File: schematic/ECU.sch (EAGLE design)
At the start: 21 parts, among them J1 Break, J2 COMM, J3 PWS, J4 DISPLAY, J5 THROTTLE, J6 LED, J7 SPEED, Q1 NMOSFETSOT23, Q2 NMOSFETSOT23, Q4 PMOSFET_BSS84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

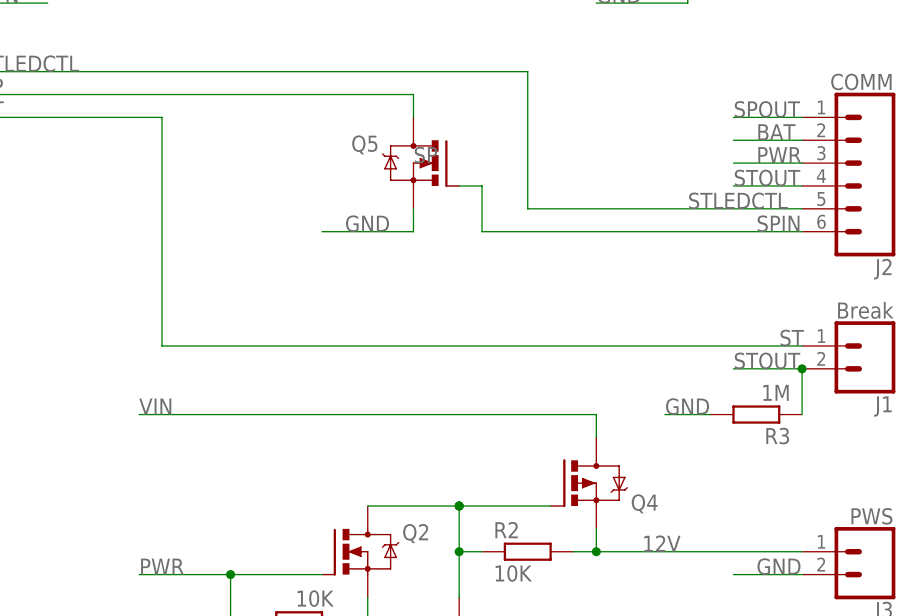
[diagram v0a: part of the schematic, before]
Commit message: Fix stop sensor schematics
- Make stop sensor LOW by default, connected to GND.
- Add control transistor for break on BLDC
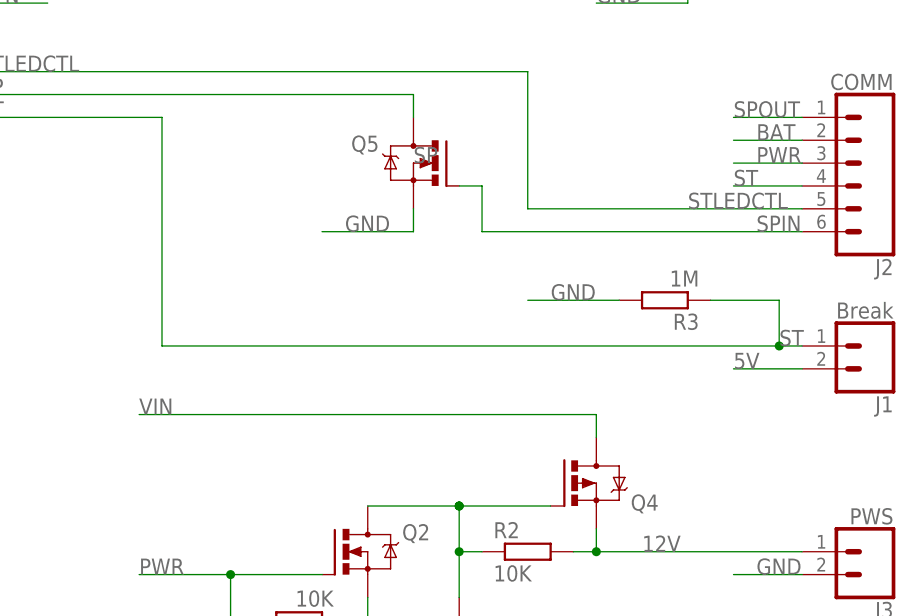
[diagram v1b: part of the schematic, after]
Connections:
- removed net STOUT: J1.2, J2.4, R3.1
- net 5V: now also J1.2
- net ST: now also J2.4, R3.1
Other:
- moved on the sheet: R3
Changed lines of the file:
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@@
 <attribute name="VALUE" x="-30.48" y="40.386" size="1.778" layer="96" font="vector" rot="MR270"/>
 </instance>
-<instance part="R3" gate="G$1" x="132.08" y="22.86" smashed="yes" rot="R180">
-<attribute name="NAME" x="135.89" y="21.3614" size="1.778" layer="95" rot="R180"/>
-<attribute name="VALUE" x="135.89" y="26.162" size="1.778" layer="96" rot="R180"/>
+<instance part="R3" gate="G$1" x="121.92" y="35.56" smashed="yes" rot="R180">
+<attribute name="NAME" x="125.73" y="34.0614" size="1.778" layer="95" rot="R180"/>
+<attribute name="VALUE" x="125.73" y="38.862" size="1.778" layer="96" rot="R180"/>
 </instance>
 </instances>
@@
 <segment>
 <pinref part="R3" gate="G$1" pin="2"/>
-<wire x1="127" y1="22.86" x2="121.92" y2="22.86" width="0.1524" layer="91"/>
-<label x="121.92" y="22.86" size="1.778" layer="95"/>
+<wire x1="116.84" y1="35.56" x2="106.68" y2="35.56" width="0.1524" layer="91"/>
+<label x="109.22" y="35.56" size="1.778" layer="95"/>
 </segment>
 </net>
@@
 <label x="10.16" y="93.98" size="1.778" layer="95"/>
 </segment>
+<segment>
+<pinref part="J1" gate="G$1" pin="2"/>
+<label x="129.54" y="27.94" size="1.778" layer="95"/>
+<wire x1="137.16" y1="27.94" x2="129.54" y2="27.94" width="0.1524" layer="91"/>
+</segment>
 </net>
 <net name="THIN" class="0">
@@
 <label x="134.62" y="30.48" size="1.778" layer="95"/>
 <label x="45.72" y="55.88" size="1.778" layer="95"/>
-<wire x1="137.16" y1="30.48" x2="66.04" y2="30.48" width="0.1524" layer="91"/>
+<wire x1="137.16" y1="30.48" x2="134.62" y2="30.48" width="0.1524" layer="91"/>
+<wire x1="134.62" y1="30.48" x2="66.04" y2="30.48" width="0.1524" layer="91"/>
 <wire x1="66.04" y1="55.88" x2="45.72" y2="55.88" width="0.1524" layer="91"/>
 <pinref part="U$2" gate="G$1" pin="D2"/>
 <wire x1="66.04" y1="55.88" x2="66.04" y2="30.48" width="0.1524" layer="91"/>
+<pinref part="R3" gate="G$1" pin="1"/>
+<wire x1="127" y1="35.56" x2="134.62" y2="35.56" width="0.1524" layer="91"/>
+<wire x1="134.62" y1="35.56" x2="134.62" y2="30.48" width="0.1524" layer="91"/>
+<junction x="134.62" y="30.48"/>
+</segment>
+<segment>
+<pinref part="J2" gate="G$1" pin="4"/>
+<wire x1="137.16" y1="48.26" x2="129.54" y2="48.26" width="0.1524" layer="91"/>
+<label x="129.54" y="48.26" size="1.778" layer="95"/>
 </segment>
 </net>
@@
 </segment>
 </net>
-<net name="STOUT" class="0">
-<segment>
-<pinref part="J1" gate="G$1" pin="2"/>
-<wire x1="137.16" y1="27.94" x2="137.16" y2="22.86" width="0.1524" layer="91"/>
-<label x="129.54" y="27.94" size="1.778" layer="95"/>
-<pinref part="R3" gate="G$1" pin="1"/>
-<wire x1="137.16" y1="27.94" x2="129.54" y2="27.94" width="0.1524" layer="91"/>
-<junction x="137.16" y="27.94"/>
-</segment>
-<segment>
-<pinref part="J2" gate="G$1" pin="4"/>
-<wire x1="137.16" y1="48.26" x2="129.54" y2="48.26" width="0.1524" layer="91"/>
-<label x="129.54" y="48.26" size="1.778" layer="95"/>
-</segment>
-</net>

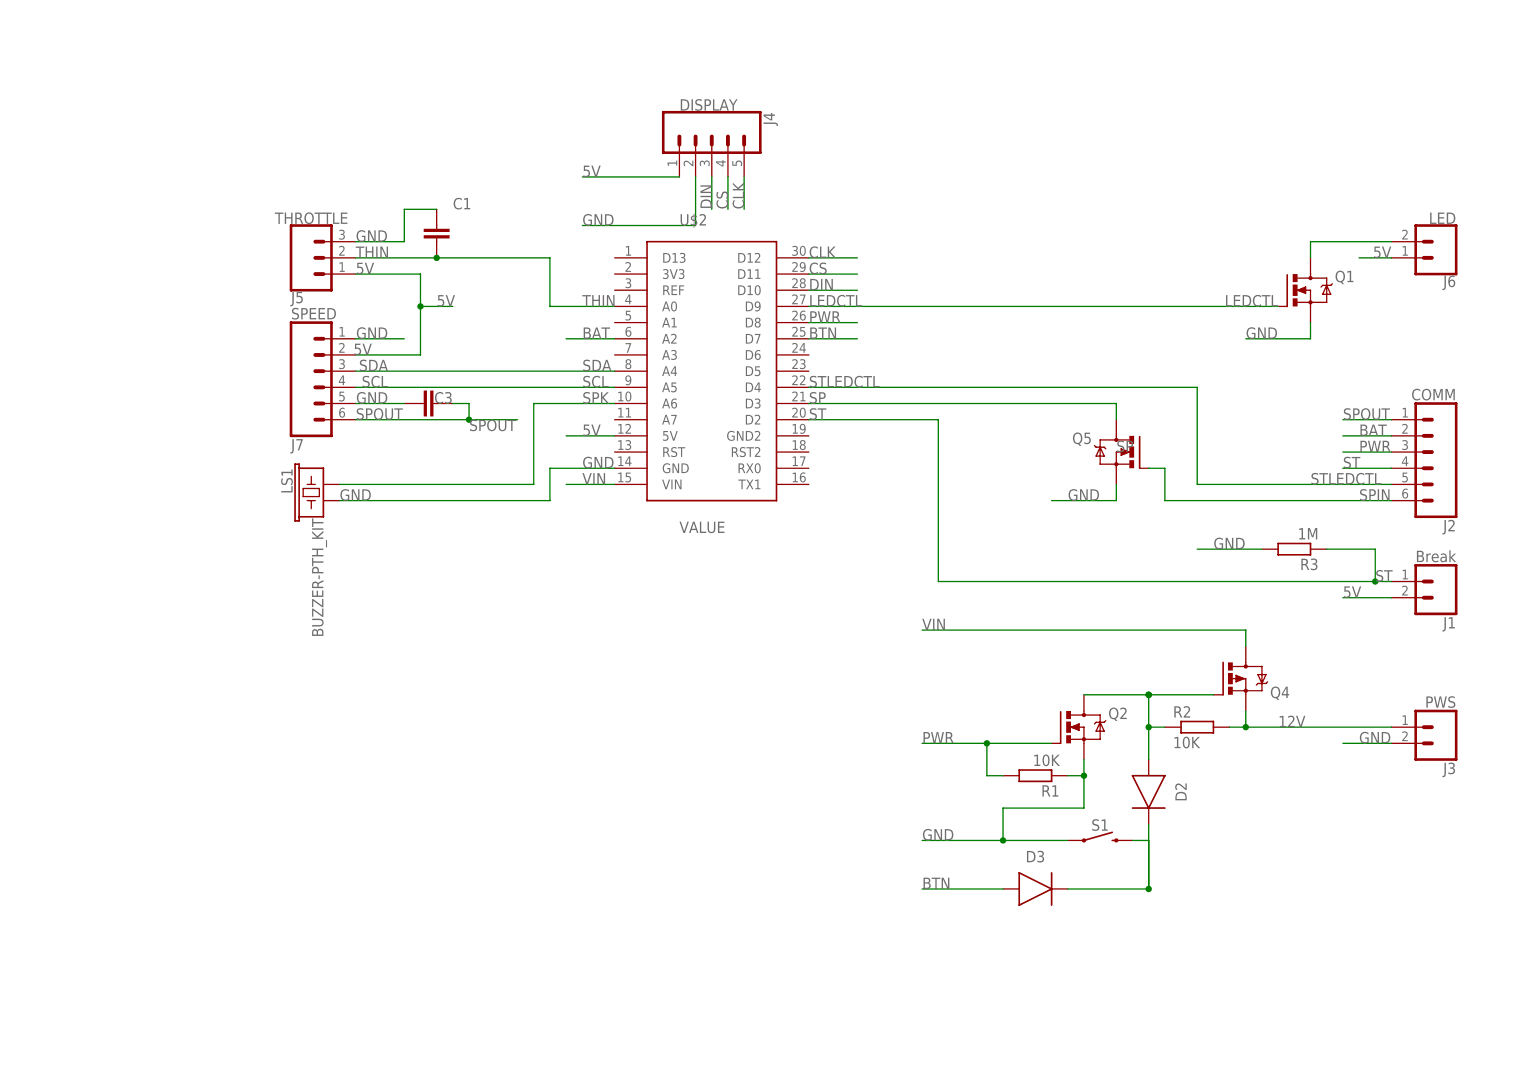
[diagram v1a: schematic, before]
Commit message: Update schematics
- Add TVS diodes for ESD protection
- Add resistors on MOSFET gates
- Make voltage divider on 2 resistors(4 previously)
- Align signal names on regulator and ECU schematics
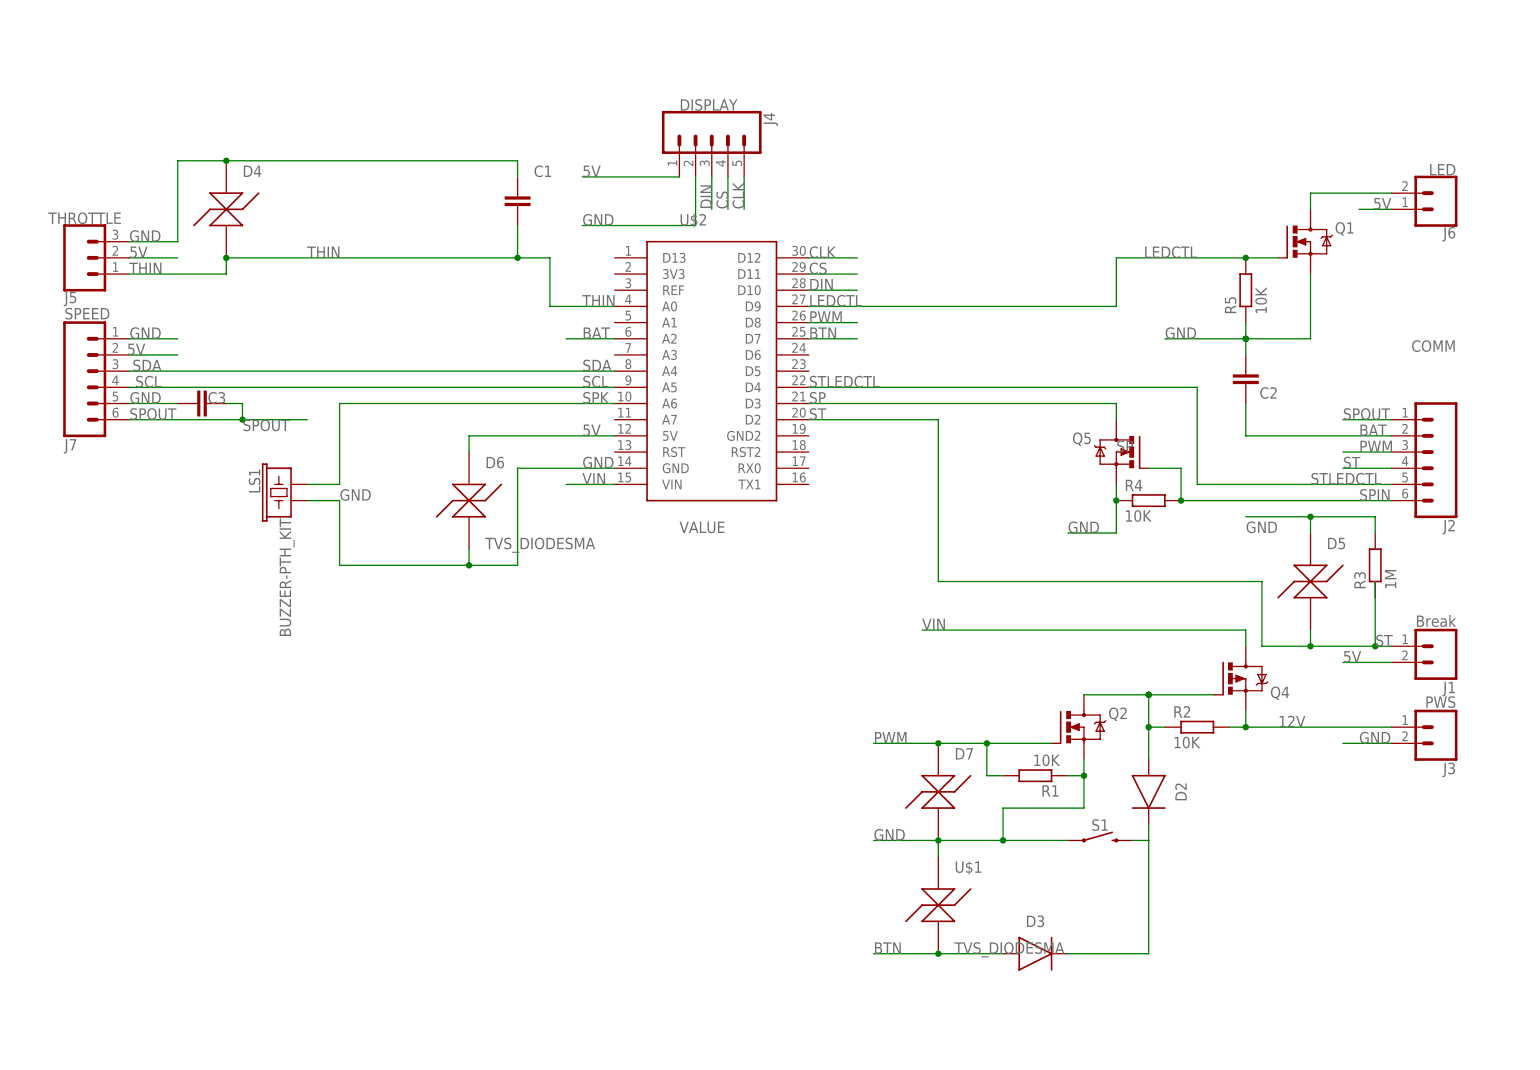
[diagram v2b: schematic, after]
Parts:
- added C2: (no value), Capacitor:C_CHIP-1206(3216-METRIC)
- added D4, D5, D6, D7, U$1: TVS_DIODESMA, eScooter:TVS_DIODESMA
- added R4, R5: 10K, eagle-ltspice:RR1206
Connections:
- removed net PWR: J2.3, Q2.G, R1.2, U$2.D8
- new net PWM: D7.P$1, J2.3, Q2.G, R1.2, U$2.D8
- net 5V: now also D6.P$1, J5.2; no longer J5.1
- net BAT: now also C2.1
- net BTN: now also U$1.P$2
- net GND: now also C2.2, D4.P$1, D5.P$1, D6.P$2, D7.P$2, R4.1, R5.1, U$1.P$1
- net LEDCTL: now also R5.2
- net SPIN: now also R4.2
- net ST: now also D5.P$2
- net THIN: now also D4.P$2, J5.1; no longer J5.2
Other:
- moved on the sheet: C1, C3, D3, J1, J5, J6, J7, LS1, Q1, R3

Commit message: Update schematics for regulator
- Add elements nominals and correct values
- Fix library inconsistence
- Few cosmetical changes in schematics
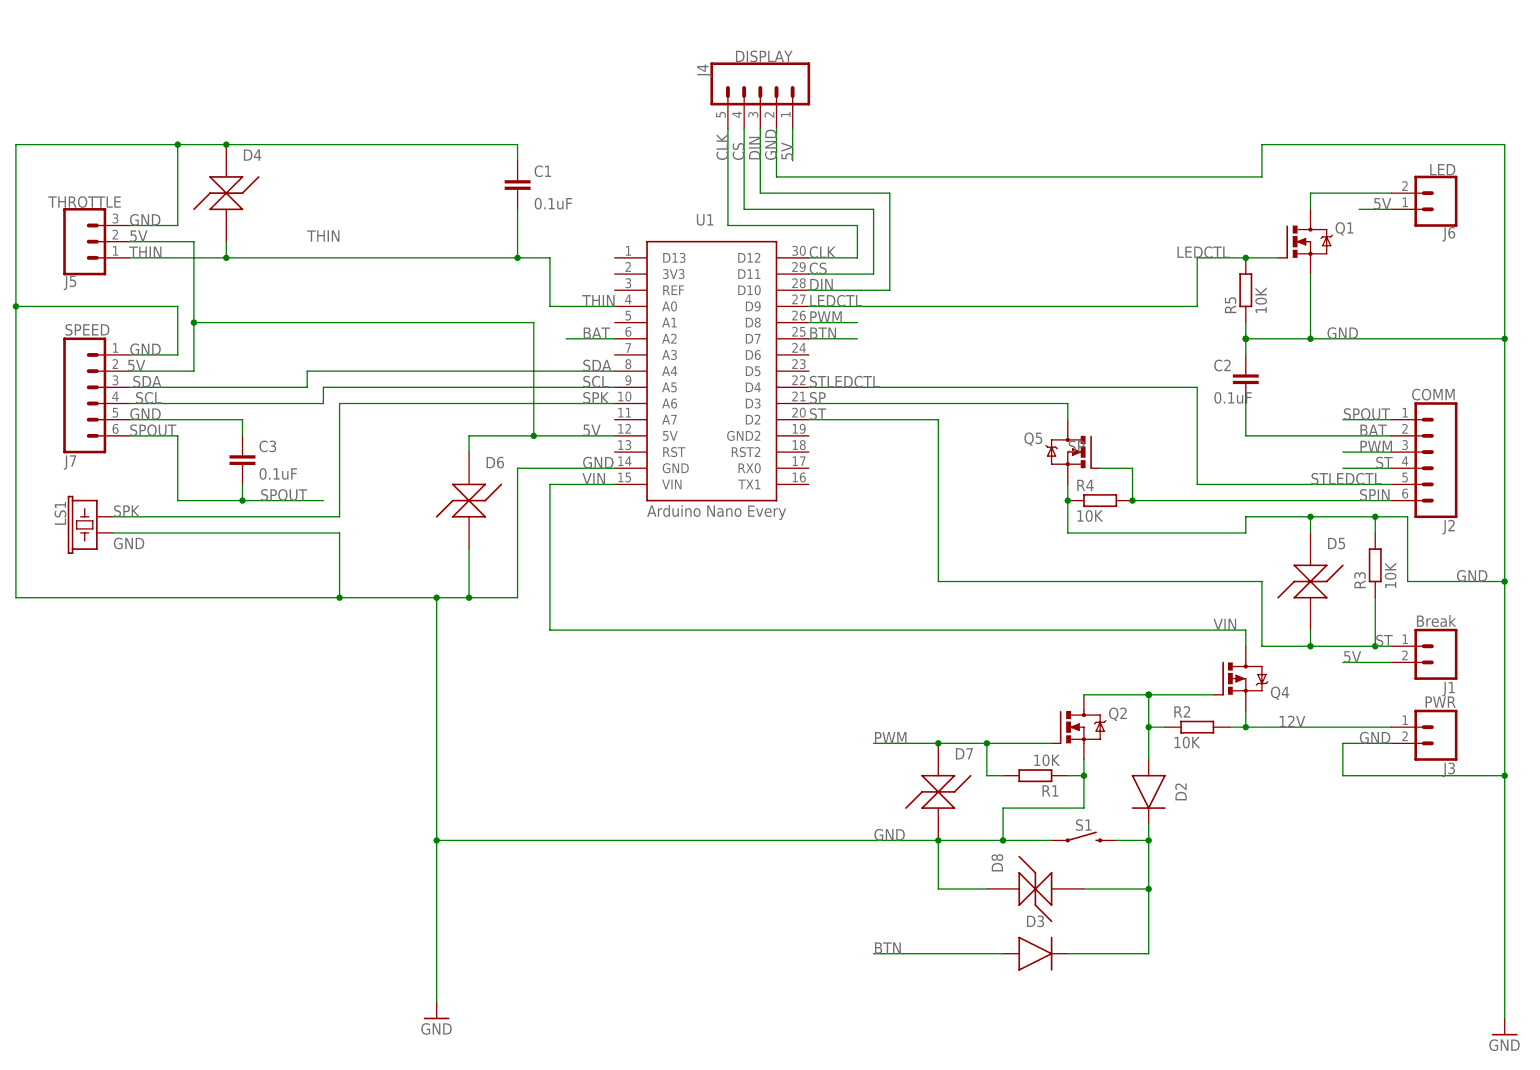
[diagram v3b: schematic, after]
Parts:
- removed U$1: TVS_DIODESMA, eScooter:TVS_DIODESMA
- removed U$2: ARDUINOARDUINO_NANO, regulator:ARDUINOARDUINO_NANO
- added D8: TVS_DIODESMA, eScooter:TVS_DIODESMA
- added U1: Arduino Nano Every, eScooter:ARDUINOARDUINO_NANO
- C1, C2, C3: value (none) -> 0.1uF
- J3: value PWS -> PWR
- R3: value 1M -> 10K
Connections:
- net 5V: now also U1.5V; no longer U$2.5V
- net BAT: now also U1.A2; no longer U$2.A2
- net BTN: now also U1.D7; no longer U$1.P$2, U$2.D7
- net CLK: now also U1.D12; no longer U$2.D12
- net CS: now also U1.D11; no longer U$2.D11
- net DIN: now also U1.D10; no longer U$2.D10
- net GND: now also D8.P$1, U1.GND; no longer U$1.P$1, U$2.GND
- net LEDCTL: now also U1.D9; no longer U$2.D9
- net N$5: now also D8.P$2
- net PWM: now also U1.D8; no longer U$2.D8
- net SCL: now also U1.A5; no longer U$2.A5
- net SDA: now also U1.A4; no longer U$2.A4
- net SP: now also U1.D3; no longer U$2.D3
- net SPK: now also U1.A6; no longer U$2.A6
- net ST: now also U1.D2; no longer U$2.D2
- net STLEDCTL: now also U1.D4; no longer U$2.D4
- net THIN: now also U1.A0; no longer U$2.A0
- net VIN: now also U1.VIN; no longer U$2.VIN
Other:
- moved on the sheet: C1, C3, D4, J4, J5, J7, LS1, Q5, R4, S1
